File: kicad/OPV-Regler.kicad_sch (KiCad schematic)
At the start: 13 parts, among them U1 TL081, U2 TL081, U3 TL081, U4 TL081

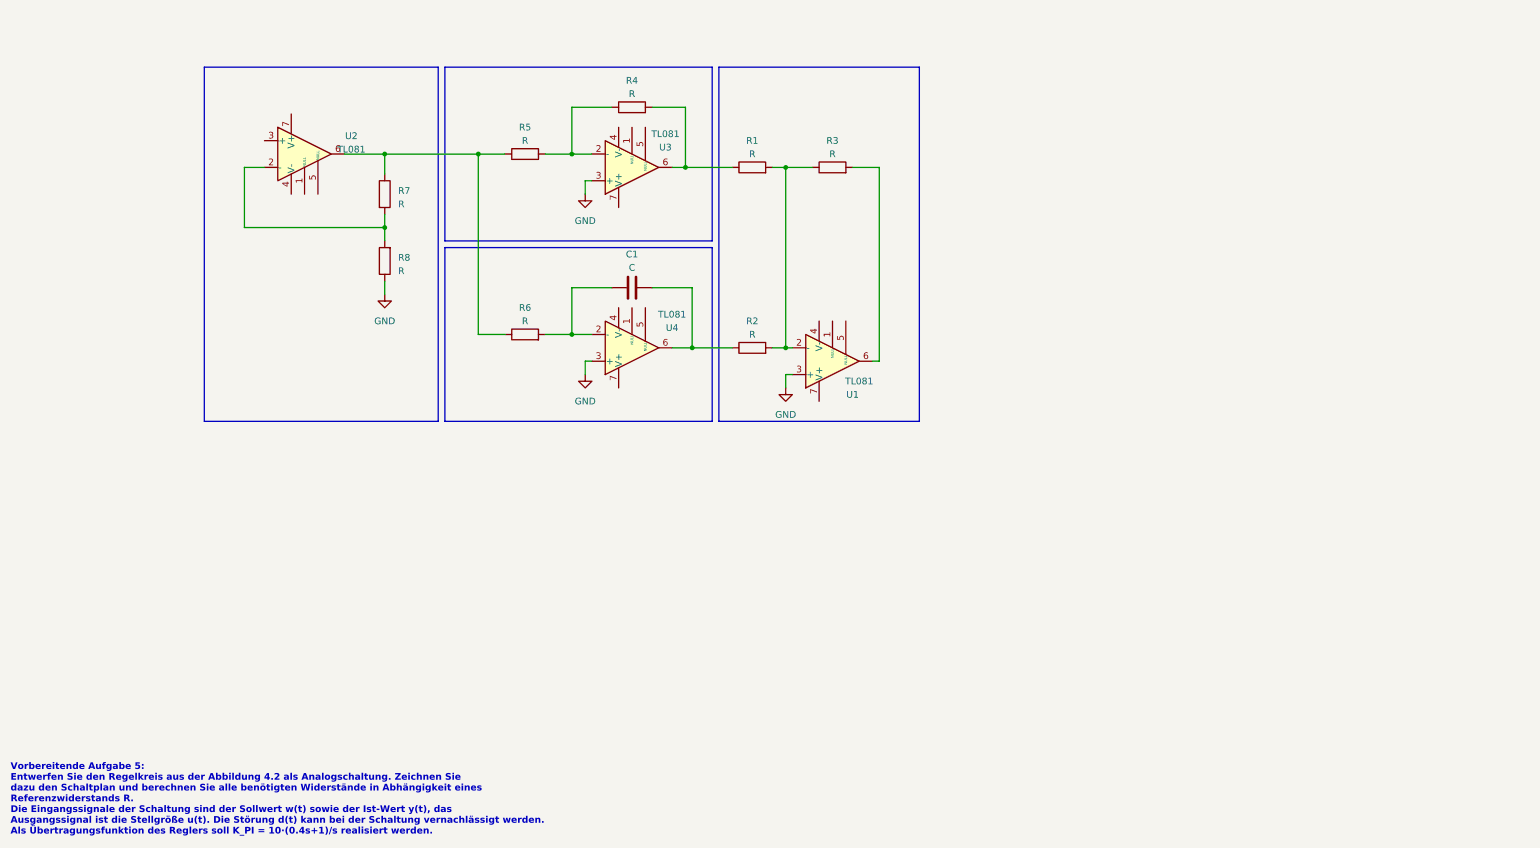
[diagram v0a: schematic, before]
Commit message: Add inputs and outputs
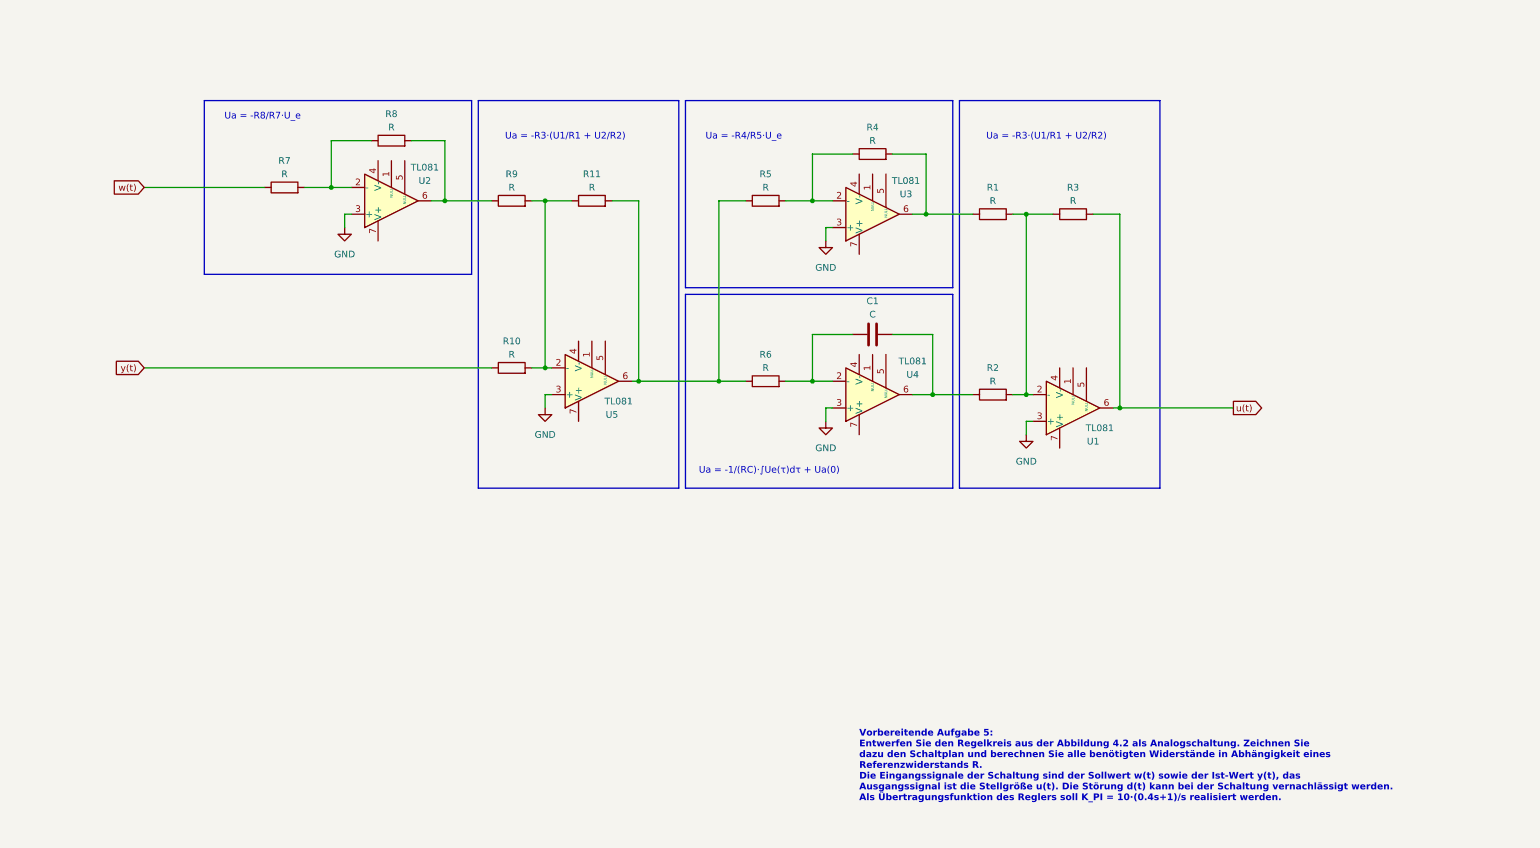
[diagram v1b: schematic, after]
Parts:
- added R10, R11, R9: R, symbol Device:R
- added U5: TL081, symbol Amplifier_Operational:TL081
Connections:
- net GND: now also U2.3 (+), U5.3 (+); no longer R8.1
- net at R5.1, R6.1: now also R11.2, U5.6; no longer R7.1, U2.6
- net at R7.2, U2.2 (-): now also R8.1; no longer R8.2
- net u(t): now reaches R3.2, U1.6
- new net: R10.2, R11.1, R9.2, U5.2 (-)
- new net: R8.2, R9.1, U2.6
- new net w(t): R7.1
- new net y(t): R10.1
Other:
- note added: "Ua = -1/(RC)·∫Ue(τ)dτ + Ua(0)"
- note added: "Ua = -R3·(U1/R1 + U2/R2)"
- note added: "Ua = -R4/R5·U_e"
- note added: "Ua = -R8/R7·U_e"
- moved on the sheet: C1, R1, R2, R3, R4, R5, R6, U1, U3, U4

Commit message: Annotate schematic
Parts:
- R11: renamed from R2; value R -> 10k
- R4: renamed from R9; value R -> 10k
- R5: renamed from R11; value R -> 10k
- R7: renamed from R1; value R -> 10k
- R8: renamed from R3; value R -> 10k
- R9: renamed from R10; value R -> 10k
- renumbered R8 to R1, R6 to R10, R4 to R2, R7 to R3, R5 to R6, U2 to U1, U3 to U2, U5 to U3, U1 to U5
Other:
- note added: "Ua = -R1/R3·U_e"
- note added: "Ua = -R2/R6·U_e"
- note removed: "Ua = -R4/R5·U_e"
- note removed: "Ua = -R8/R7·U_e"

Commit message: Add schaltplan pdf
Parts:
- added R12: 10k, symbol Device:R
- C1: value C -> 470n
- R1: value R -> 22k + 1k5
- R10: value R -> 8M2 + 330k
- R2: value R -> 39k + 1k
- R3, R6: value R -> 10k
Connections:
- net at C1.1, R10.2, U4.2 (-): now also R12.1
- net at C1.2, R11.1, U4.6: now also R12.2
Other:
- note added: "G = -2,35"
- note added: "G = -40"
- note added: "RC = 4s"
- note added: "Vorgabe: Kondensator 470 nF"
- note added: "Widerstände nach Reihe E12"
- company: (none) -> Universität Ulm
- title: (none) -> ERT-Praktikum - Aufgabe 5: PI-Regler
- moved on the sheet: C1, R1, R10, R11, R2, R3, R4, R5, R6, R7, R8, R9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

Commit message: Update op-amp 1 gain
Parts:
- R1: value 22k + 1k5 -> 4k7
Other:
- note added: "G = -0,425"
- note removed: "G = -2,35"
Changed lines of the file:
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@@
     (effects (font (size 1.27 1.27)) (justify left bottom))
   )
-  (text "G = -2,35" (at 57.15 74.93 0)
+  (text "G = -0,425" (at 57.15 74.93 0)
     (effects (font (size 1.27 1.27)) (justify left bottom))
   )
@@
       (effects (font (size 1.27 1.27)))
     )
-    (property "Value" "22k + 1k5" (at 88.9 72.39 90)
-      (effects (font (size 1.27 1.27)))
-    )
+    (property "Value" "4k7" (at 88.9 72.39 90)
+      (effects (font (size 1.27 1.27)))
+    )
